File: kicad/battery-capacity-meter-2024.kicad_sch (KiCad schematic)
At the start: 77 parts, among them J3 Conn_MainBoard, J4 Conn_DisplayBoard, J5 PWR, Q1 2N3904, Q2 2N3906, Q3 2SD2390, Q6 X0402MF, SW1 CHARGE/DISCHARGE, SW2 1A MODE, U1 LM2596_StepDown_Module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

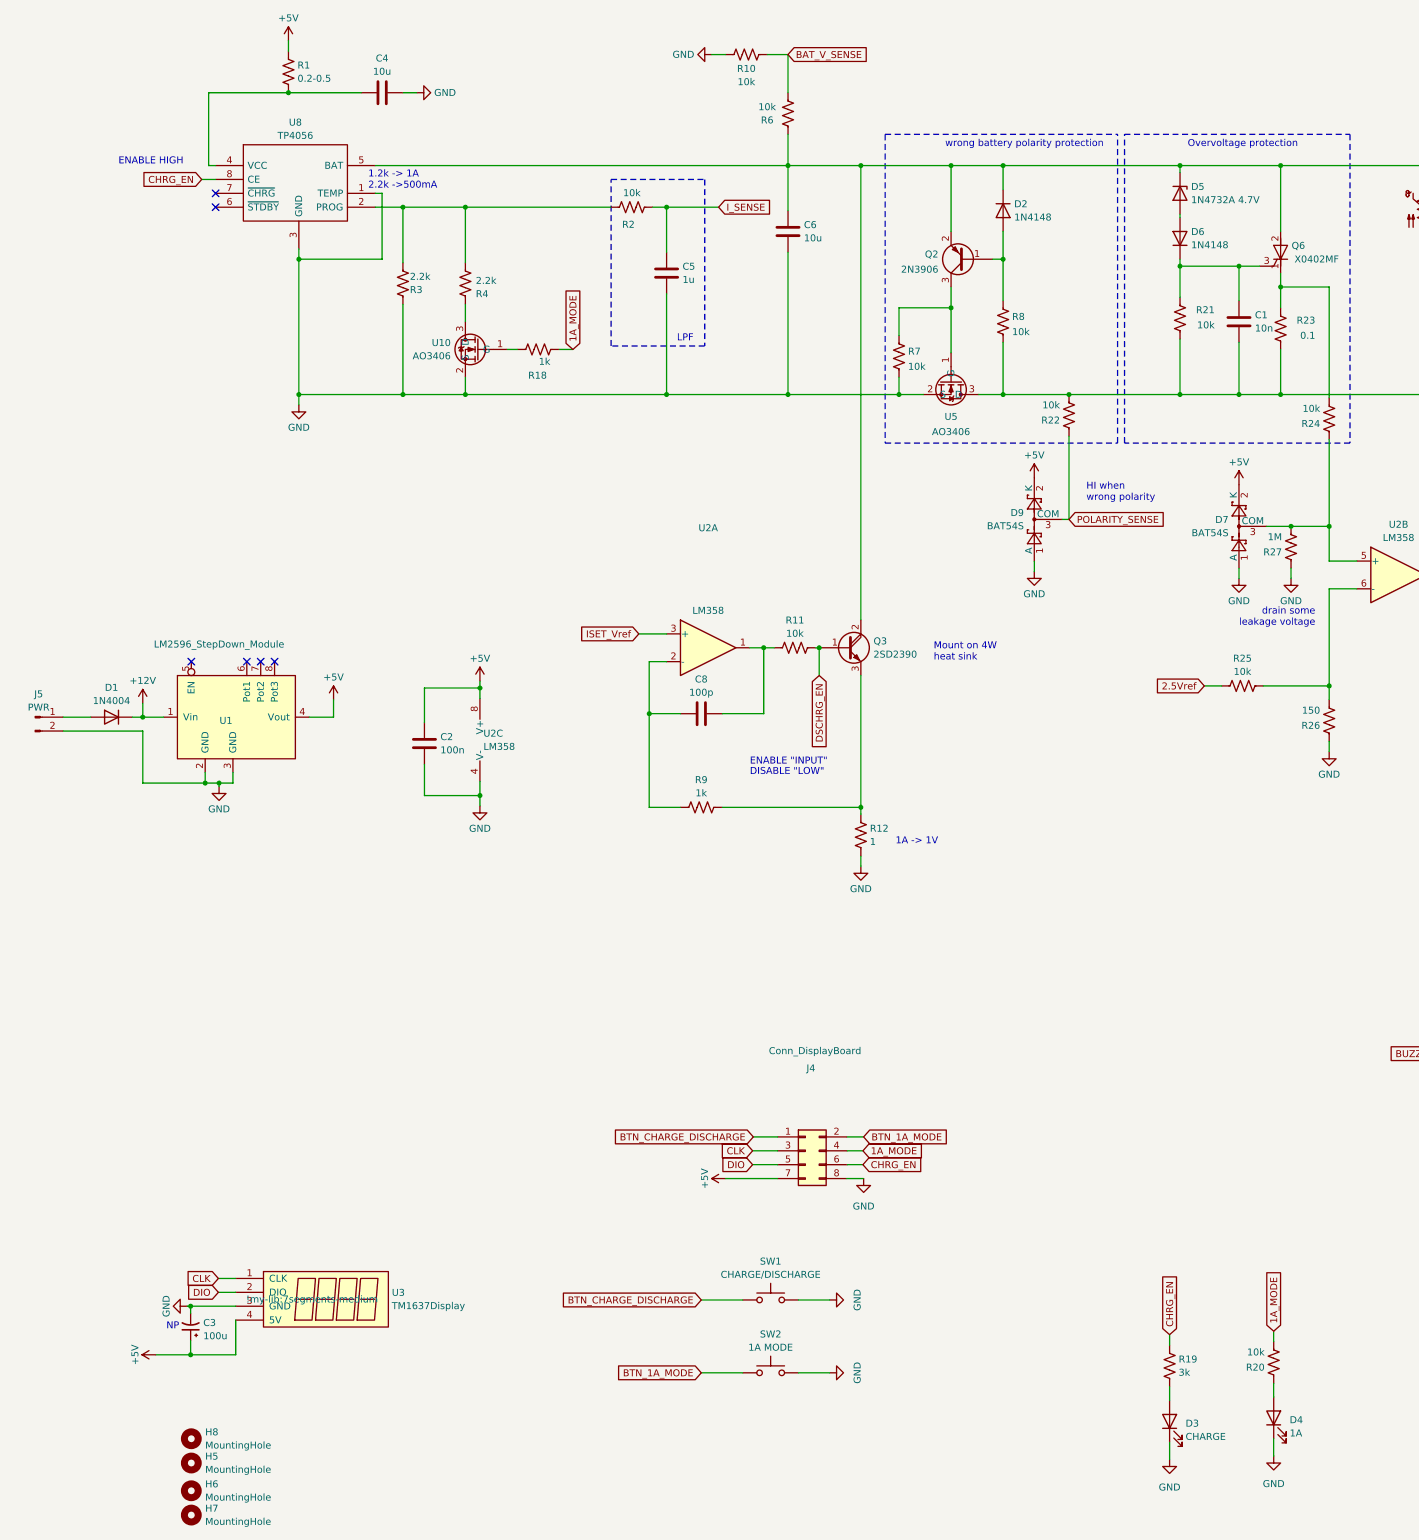
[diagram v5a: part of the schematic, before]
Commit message: ready two layers
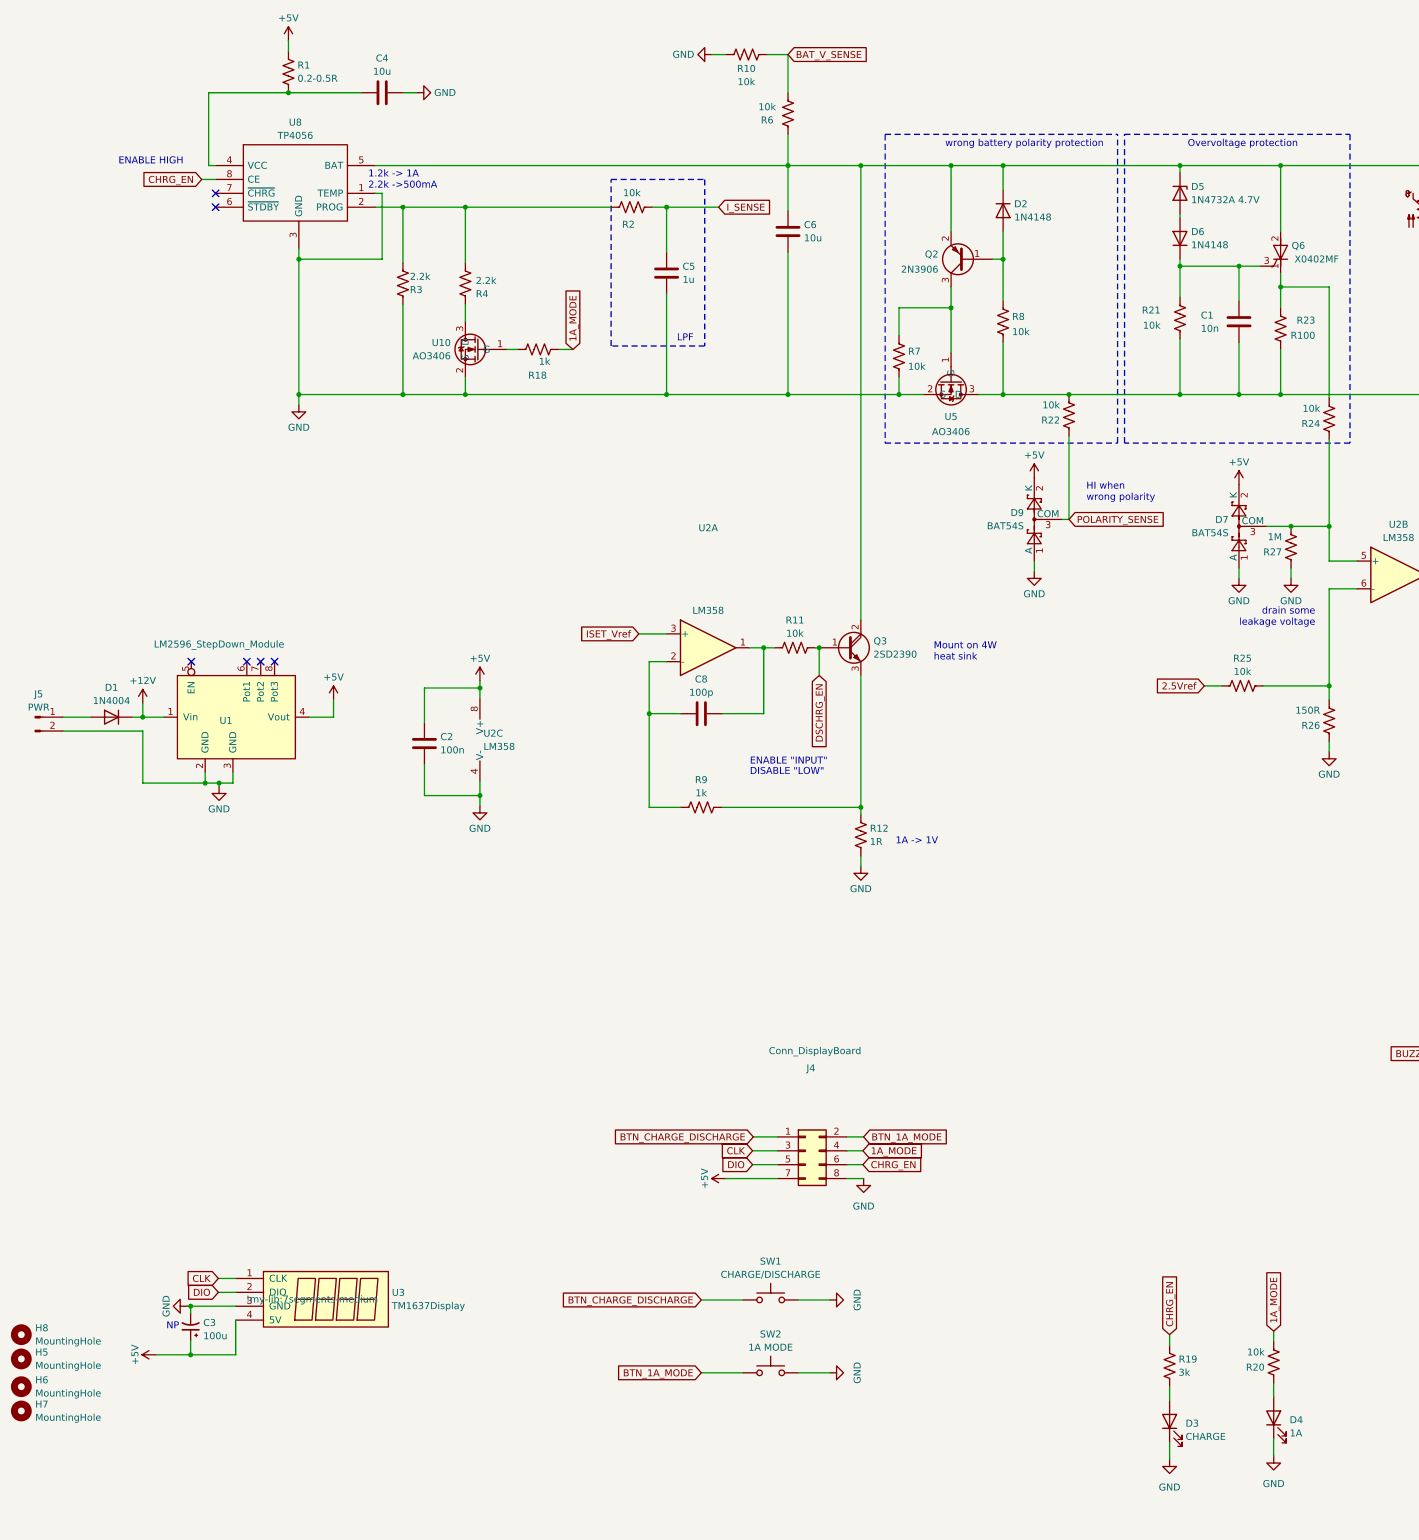
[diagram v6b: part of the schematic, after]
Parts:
- R1: value 0.2-0.5 -> 0.2-0.5R
- R12: value 1 -> 1R
- R23: value 0.1 -> R100
- R26: value 150 -> 150R
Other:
- moved on the sheet: H5, H6, H7, H8
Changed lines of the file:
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@@
       (effects (font (size 1.27 1.27)) (justify right))
     )
-    (property "Value" "150" (at 258.064 142.2784 0)
+    (property "Value" "150R" (at 258.064 142.2784 0)
       (effects (font (size 1.27 1.27)) (justify right))
     )
@@
     )
   )
-  (symbol (lib_id "Mechanical:MountingHole") (at 51.435 285.115 0) (unit 1)
-    (in_bom yes) (on_board yes) (dnp no) (fields_autoplaced)
-    (property "Reference" "H6" (at 53.975 283.9029 0)
-      (effects (font (size 1.27 1.27)) (justify left))
-    )
-    (property "Value" "MountingHole" (at 53.975 286.3271 0)
-      (effects (font (size 1.27 1.27)) (justify left))
-    )
-    (property "Footprint" "MountingHole:MountingHole_2.2mm_M2" (at 51.435 285.115 0)
-      (effects (font (size 1.27 1.27)) hide)
-    )
-    (property "Datasheet" "~" (at 51.435 285.115 0)
+  (symbol (lib_id "Mechanical:MountingHole") (at 20.32 266.065 0) (unit 1)
+    (in_bom yes) (on_board yes) (dnp no) (fields_autoplaced)
+    (property "Reference" "H6" (at 22.86 264.8529 0)
+      (effects (font (size 1.27 1.27)) (justify left))
+    )
+    (property "Value" "MountingHole" (at 22.86 267.2771 0)
+      (effects (font (size 1.27 1.27)) (justify left))
+    )
+    (property "Footprint" "MountingHole:MountingHole_2.2mm_M2" (at 20.32 266.065 0)
+      (effects (font (size 1.27 1.27)) hide)
+    )
+    (property "Datasheet" "~" (at 20.32 266.065 0)
       (effects (font (size 1.27 1.27)) hide)
     )
@@
     )
   )
-  (symbol (lib_id "Mechanical:MountingHole") (at 51.435 289.56 0) (unit 1)
-    (in_bom yes) (on_board yes) (dnp no) (fields_autoplaced)
-    (property "Reference" "H7" (at 53.975 288.3479 0)
-      (effects (font (size 1.27 1.27)) (justify left))
-    )
-    (property "Value" "MountingHole" (at 53.975 290.7721 0)
-      (effects (font (size 1.27 1.27)) (justify left))
-    )
-    (property "Footprint" "MountingHole:MountingHole_2.2mm_M2" (at 51.435 289.56 0)
-      (effects (font (size 1.27 1.27)) hide)
-    )
-    (property "Datasheet" "~" (at 51.435 289.56 0)
+  (symbol (lib_id "Mechanical:MountingHole") (at 20.32 270.51 0) (unit 1)
+    (in_bom yes) (on_board yes) (dnp no) (fields_autoplaced)
+    (property "Reference" "H7" (at 22.86 269.2979 0)
+      (effects (font (size 1.27 1.27)) (justify left))
+    )
+    (property "Value" "MountingHole" (at 22.86 271.7221 0)
+      (effects (font (size 1.27 1.27)) (justify left))
+    )
+    (property "Footprint" "MountingHole:MountingHole_2.2mm_M2" (at 20.32 270.51 0)
+      (effects (font (size 1.27 1.27)) hide)
+    )
+    (property "Datasheet" "~" (at 20.32 270.51 0)
       (effects (font (size 1.27 1.27)) hide)
     )
@@
     )
   )
-  (symbol (lib_id "Mechanical:MountingHole") (at 51.435 280.035 0) (unit 1)
-    (in_bom yes) (on_board yes) (dnp no) (fields_autoplaced)
-    (property "Reference" "H5" (at 53.975 278.8229 0)
-      (effects (font (size 1.27 1.27)) (justify left))
-    )
-    (property "Value" "MountingHole" (at 53.975 281.2471 0)
-      (effects (font (size 1.27 1.27)) (justify left))
-    )
-    (property "Footprint" "MountingHole:MountingHole_2.2mm_M2" (at 51.435 280.035 0)
-      (effects (font (size 1.27 1.27)) hide)
-    )
-    (property "Datasheet" "~" (at 51.435 280.035 0)
+  (symbol (lib_id "Mechanical:MountingHole") (at 20.32 260.985 0) (unit 1)
+    (in_bom yes) (on_board yes) (dnp no) (fields_autoplaced)
+    (property "Reference" "H5" (at 22.86 259.7729 0)
+      (effects (font (size 1.27 1.27)) (justify left))
+    )
+    (property "Value" "MountingHole" (at 22.86 262.1971 0)
+      (effects (font (size 1.27 1.27)) (justify left))
+    )
+    (property "Footprint" "MountingHole:MountingHole_2.2mm_M2" (at 20.32 260.985 0)
+      (effects (font (size 1.27 1.27)) hide)
+    )
+    (property "Datasheet" "~" (at 20.32 260.985 0)
       (effects (font (size 1.27 1.27)) hide)
     )
@@
       (effects (font (size 1.27 1.27)) (justify right))
     )
-    (property "Value" "0.1" (at 257.175 73.66 0)
+    (property "Value" "R100" (at 257.175 73.66 0)
       (effects (font (size 1.27 1.27)) (justify right))
     )
@@
   )
   (symbol (lib_id "Device:C") (at 243.205 71.12 0) (unit 1)
-    (in_bom yes) (on_board yes) (dnp no) (fields_autoplaced)
-    (property "Reference" "C1" (at 246.126 69.9079 0)
-      (effects (font (size 1.27 1.27)) (justify left))
-    )
-    (property "Value" "10n" (at 246.126 72.3321 0)
+    (in_bom yes) (on_board yes) (dnp no)
+    (property "Reference" "C1" (at 236.22 69.9658 0)
+      (effects (font (size 1.27 1.27)) (justify left))
+    )
+    (property "Value" "10n" (at 236.22 72.39 0)
       (effects (font (size 1.27 1.27)) (justify left))
     )
@@
       (effects (font (size 1.27 1.27)) (justify right))
     )
-    (property "Value" "1" (at 175.641 166.3121 0)
+    (property "Value" "1R" (at 175.641 166.3121 0)
       (effects (font (size 1.27 1.27)) (justify right))
     )
@@
       (effects (font (size 1.27 1.27)) (justify left))
     )
-    (property "Value" "0.2-0.5" (at 70.866 26.6121 0)
+    (property "Value" "0.2-0.5R" (at 70.866 26.6121 0)
       (effects (font (size 1.27 1.27)) (justify left))
     )
@@
   (symbol (lib_id "Device:R_US") (at 232.41 70.485 0) (unit 1)
     (in_bom yes) (on_board yes) (dnp no)
-    (property "Reference" "R21" (at 238.76 68.9799 0)
-      (effects (font (size 1.27 1.27)) (justify right))
-    )
-    (property "Value" "10k" (at 238.76 71.755 0)
+    (property "Reference" "R21" (at 228.854 69.0378 0)
+      (effects (font (size 1.27 1.27)) (justify right))
+    )
+    (property "Value" "10k" (at 228.854 71.8129 0)
       (effects (font (size 1.27 1.27)) (justify right))
     )
@@
     )
   )
-  (symbol (lib_id "Mechanical:MountingHole") (at 51.435 275.59 0) (unit 1)
-    (in_bom yes) (on_board yes) (dnp no) (fields_autoplaced)
-    (property "Reference" "H8" (at 53.975 274.3779 0)
-      (effects (font (size 1.27 1.27)) (justify left))
-    )
-    (property "Value" "MountingHole" (at 53.975 276.8021 0)
-      (effects (font (size 1.27 1.27)) (justify left))
-    )
-    (property "Footprint" "MountingHole:MountingHole_2.2mm_M2" (at 51.435 275.59 0)
-      (effects (font (size 1.27 1.27)) hide)
-    )
-    (property "Datasheet" "~" (at 51.435 275.59 0)
-      (effects (font (size 1.27 1.27)) hide)
-    )
+  (symbol (lib_id "Mechanical:MountingHole") (at 20.32 256.54 0) (unit 1)
+    (in_bom yes) (on_board yes) (dnp no) (fields_autoplaced)
+    (property "Reference" "H8" (at 22.86 255.3279 0)
+      (effects (font (size 1.27 1.27)) (justify left))
+    )
+    (property "Value" "MountingHole" (at 22.86 257.7521 0)
+      (effects (font (size 1.27 1.27)) (justify left))
+    )
+    (property "Footprint" "MountingHole:MountingHole_2.2mm_M2" (at 20.32 256.54 0)
+      (effects (font (size 1.27 1.27)) hide)
+    )
+    (property "Datasheet" "~" (at 20.32 256.54 0)
+      (effects (font (size 1.27 1.27)) hide)
+    )

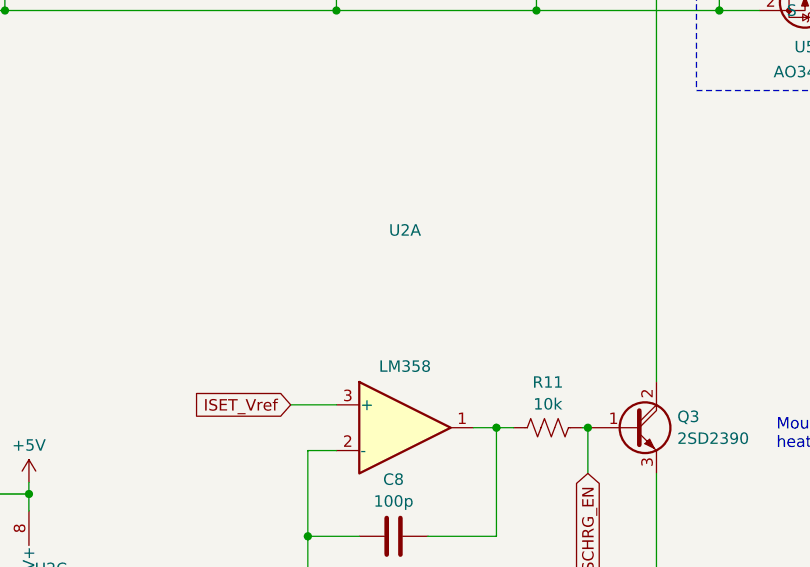
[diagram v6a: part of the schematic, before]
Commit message: fix missing pcb track
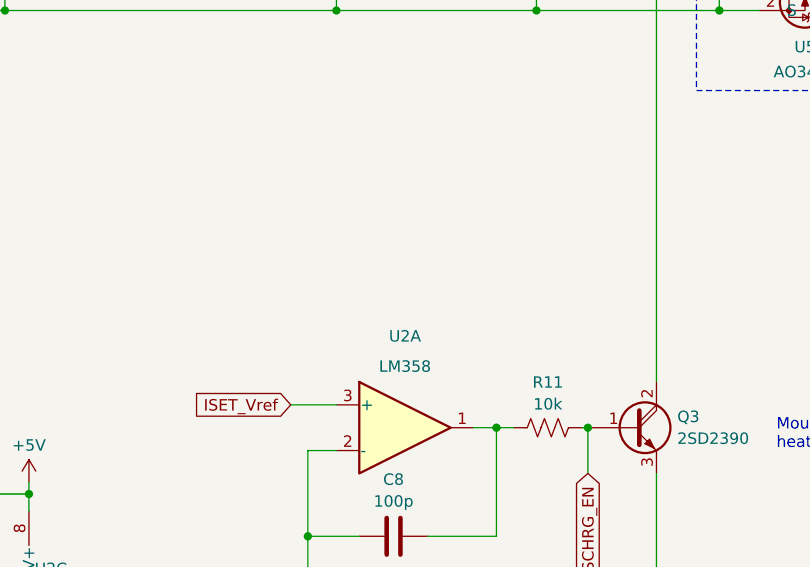
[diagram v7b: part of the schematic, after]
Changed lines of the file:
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@@
       (effects (font (size 1.27 1.27) italic) (justify left) hide)
     )
-    (property "Datasheet" "https://www.st.com/resource/en/datasheet/x02.pdf" (at 250.825 58.42 0)
+    (property "Datasheet" "https://mm.digikey.com/Volume0/opasdata/d220001/medias/docus/402/X04_Series_Ed3_Sep2000.pdf" (at 250.825 58.42 0)
       (effects (font (size 1.27 1.27)) (justify left) hide)
     )
@@
   (symbol (lib_id "Amplifier_Operational:LM358") (at 146.05 130.81 0) (unit 1)
     (in_bom yes) (on_board yes) (dnp no)
-    (property "Reference" "U2" (at 146.05 108.8857 0)
-      (effects (font (size 1.27 1.27)))
-    )
+    (property "Reference" "U2" (at 146.05 120.65 0)
+      (effects (font (size 1.27 1.27)))
+    )
